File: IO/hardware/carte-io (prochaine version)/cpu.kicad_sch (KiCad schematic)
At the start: 24 parts, among them J3 FTSH-105-01-L-DH, SW1 SW_Push, SW2 SW_Push, U1 STM32U545VETx, X1 ASE-16.000MHZ-LC-T

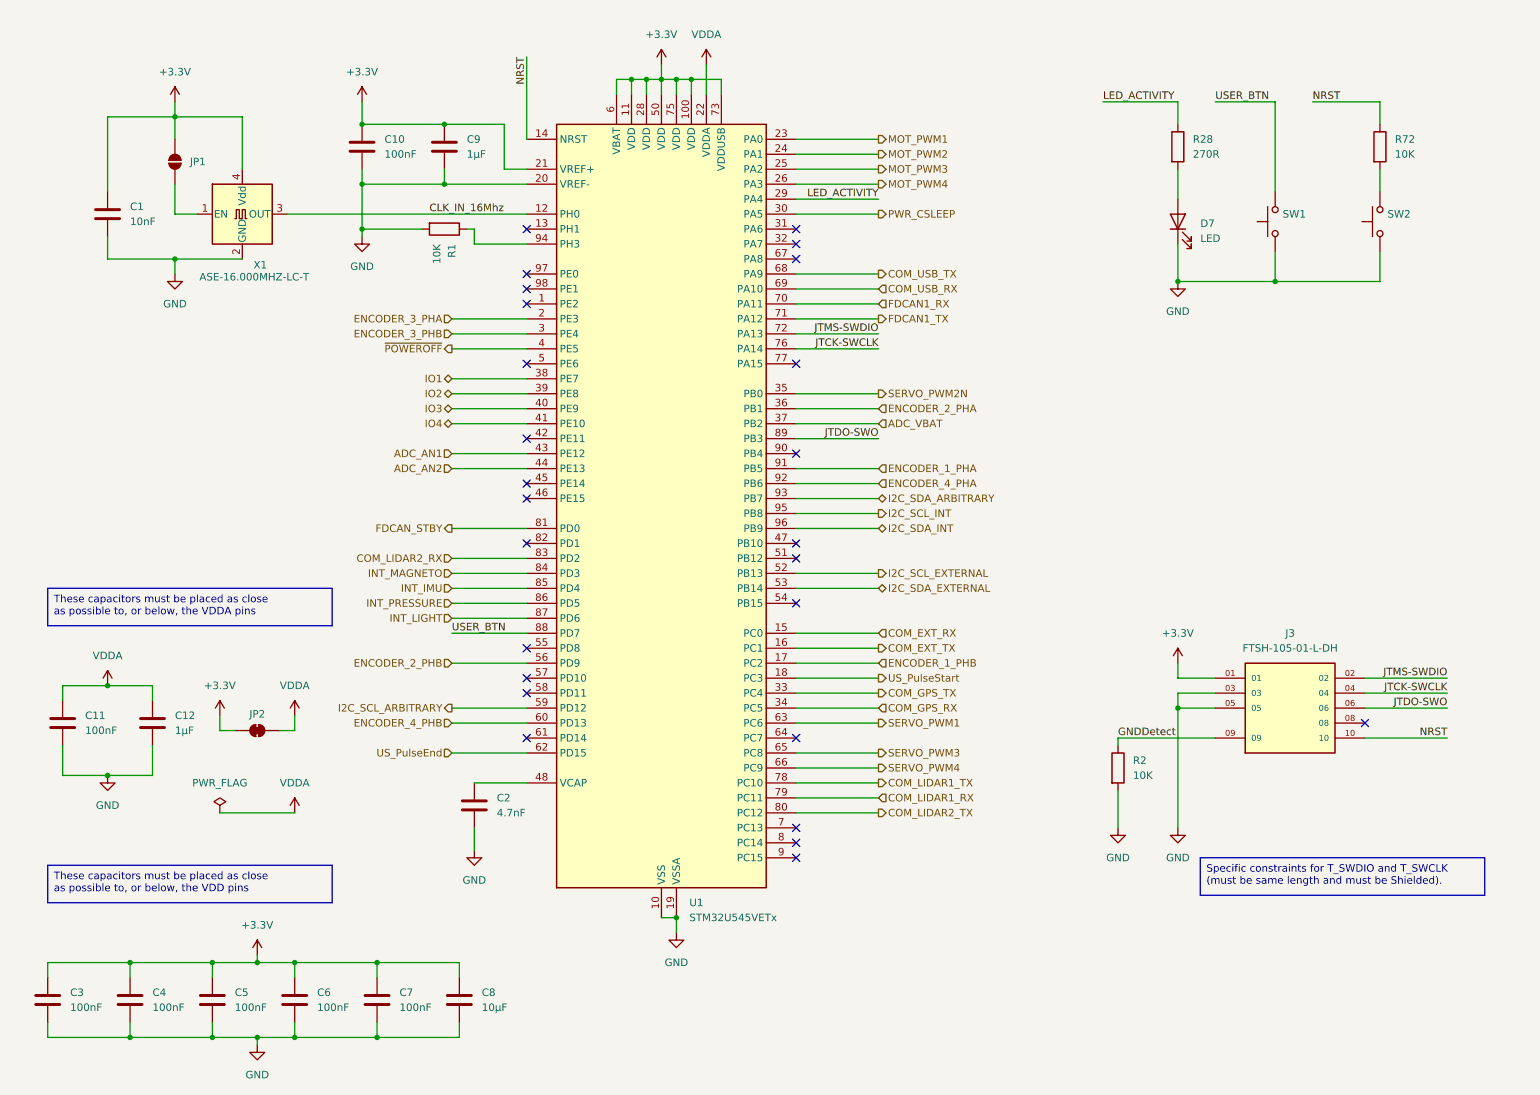
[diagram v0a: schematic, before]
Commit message: Recuperation de la carte IO perdue lors de la suppression des 3 derniers commit
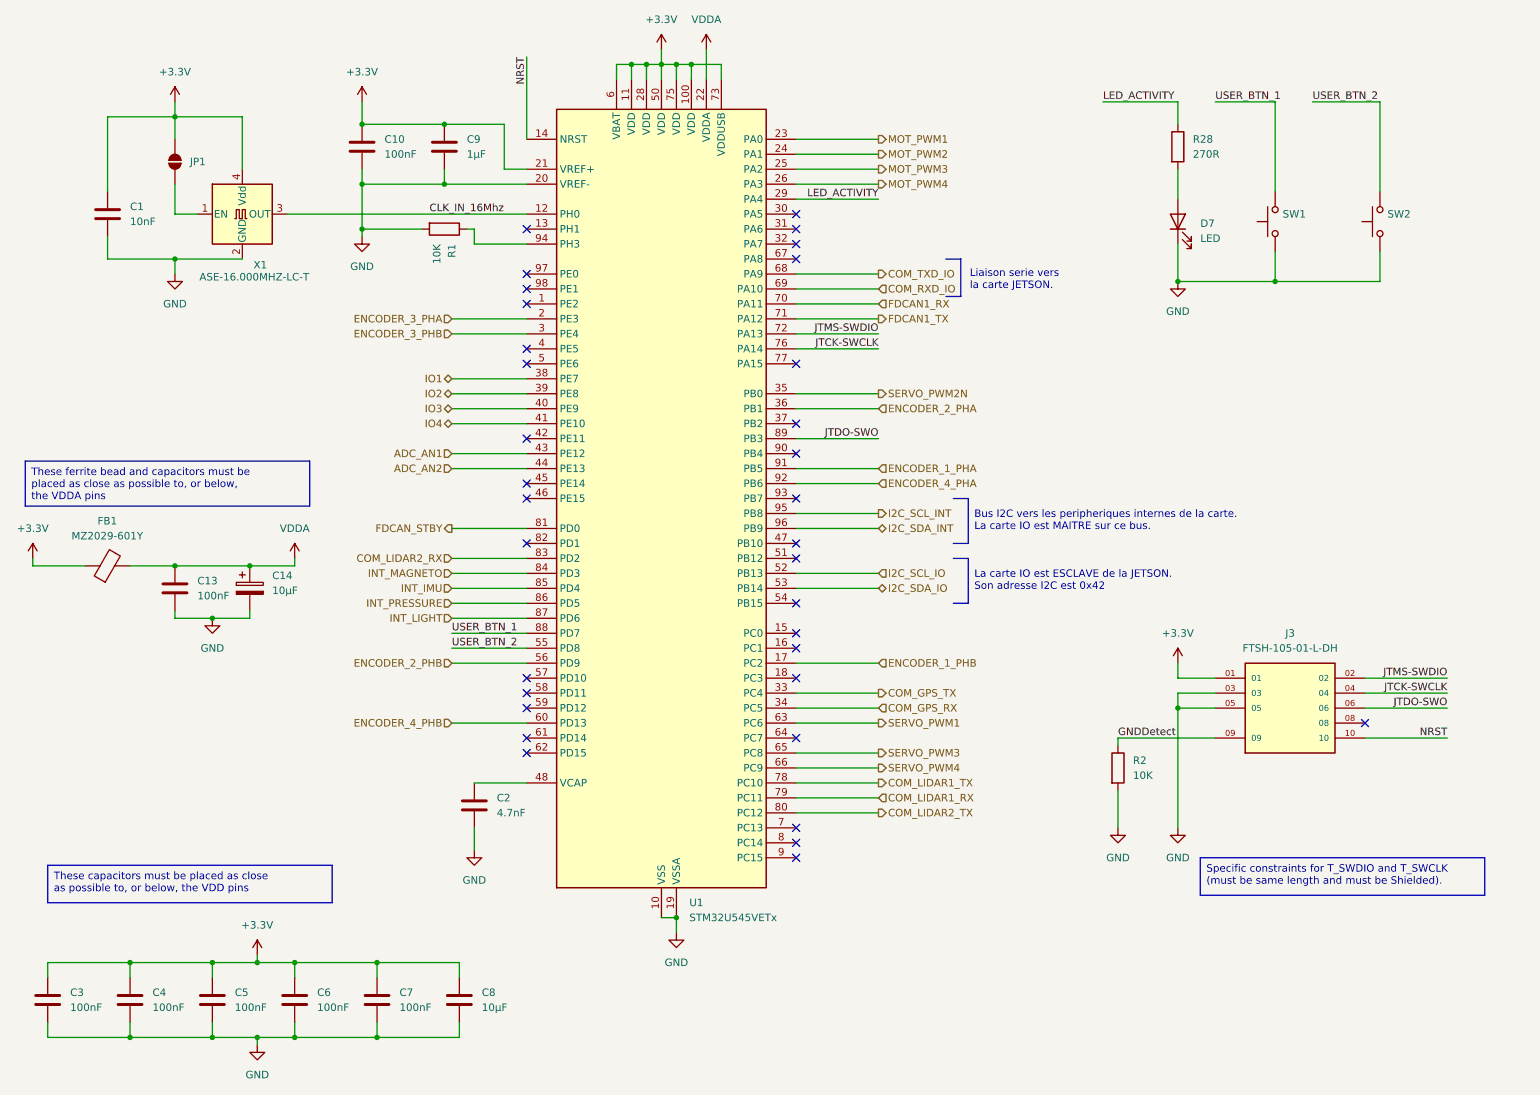
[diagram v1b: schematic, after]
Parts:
- removed C11: 100nF, Capacitor_SMD:C_0805_2012Metric_Pad1.18x1.45mm_HandSolder, symbol Device:C
- removed C12: 1µF, Capacitor_SMD:C_0805_2012Metric_Pad1.18x1.45mm_HandSolder, symbol Device:C
- removed JP2: SolderJumper_2_Bridged, Jumper:SolderJumper-2_P1.3mm_Bridged_RoundedPad1.0x1.5mm, symbol Jumper:SolderJumper_2_Bridged
- removed R72: 10K, Resistor_SMD:R_0805_2012Metric_Pad1.20x1.40mm_HandSolder, symbol Device:R
- added C13: 100nF, Capacitor_SMD:C_0805_2012Metric, symbol Device:C
- added C14: 10µF, Capacitor_SMD:C_1206_3216Metric, symbol Device:C_Polarized
- added FB1: MZ2029-601Y, Inductor_SMD:L_Eaton_MCL2012V1, symbol Device:FerriteBead
- SW1, SW2: footprint Button_Switch_SMD:Panasonic_EVQPUJ_EVQPUA -> 2-1825027-0:218250270
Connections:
- net +3.3V: now also FB1.1
- net GND: now also C13.2, C14.2
- net VDDA: now also C13.1, C14.1, FB1.2
- net USER_BTN_2: now reaches SW2.2
- net USER_BTN_2: now also U1.55 (PD8)
- net ADC_VBAT: no longer names the net of U1.37 (PB2)
- net COM_EXT_RX: no longer names the net of U1.15 (PC0)
- net COM_EXT_TX: no longer names the net of U1.16 (PC1)
- net COM_USB_RX renamed COM_RXD_IO
- net COM_USB_TX renamed COM_TXD_IO
- net I2C_SCL_ARBITRARY: no longer names the net of U1.59 (PD12)
- net I2C_SCL_EXTERNAL renamed I2C_SCL_IO
- net I2C_SDA_ARBITRARY: no longer names the net of U1.93 (PB7)
- net I2C_SDA_EXTERNAL renamed I2C_SDA_IO
- net PWR_CSLEEP: no longer names the net of U1.30 (PA5)
- net USER_BTN renamed USER_BTN_1
- net US_PulseEnd: no longer names the net of U1.62 (PD15)
- net US_PulseStart: no longer names the net of U1.18 (PC3)
- net ~{POWEROFF}: no longer names the net of U1.4 (PE5)
- no-connect marks 26 -> 34
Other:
- note added: "Bus I2C vers les peripheriques internes de la carte. La carte IO est MAITRE sur ce bus."
- note added: "La carte IO est ESCLAVE de la JETSON. Son adresse I2C est 0x42"
- note added: "Liaison serie vers la carte JETSON."
